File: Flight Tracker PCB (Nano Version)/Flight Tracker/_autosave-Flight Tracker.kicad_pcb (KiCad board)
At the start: 2 copper layers, 101.1 x 78.8 mm, 53 parts, among them J1 Conn_01x02, J2 Conn_01x02, J3 Screw_Terminal_01x02, J4 Conn_01x02, J5 Conn_01x03, J6 Conn_02x03_Odd_Even, Q1 BSS138, Q2 BSS138, Q3 BSS138, Q4 BSS138, Q5 BSS138, Q6 BSS138, Q7 FQP47P06, Q8 BSS138, Q9 BSS138, U1 ML8511, U2 BH1750, U3 SMA_5pin, U4 NTX2_With_Model, U5 BMP280, U6 MPU_9250, U7 UBlox_MAX8

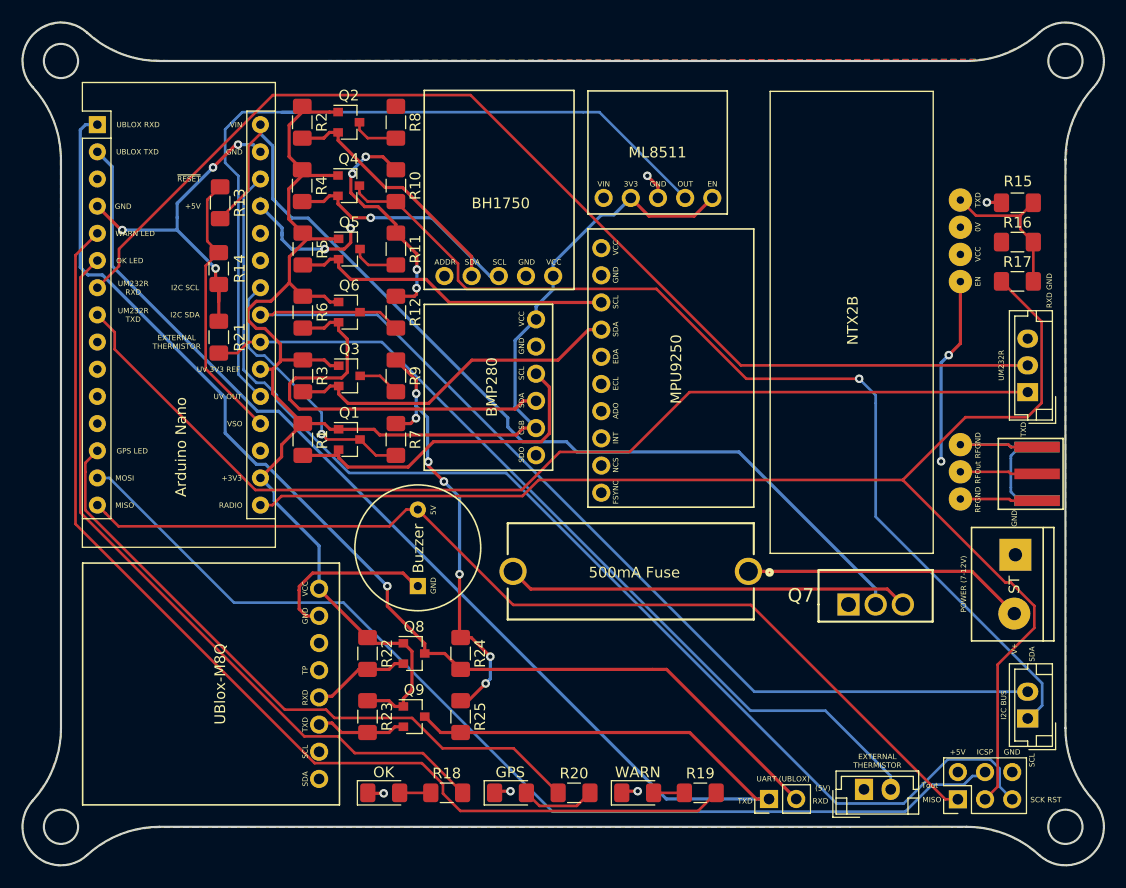
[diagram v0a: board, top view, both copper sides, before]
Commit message: made bmp280 cad model and linked it to pcb, also created sockets for arduino nano
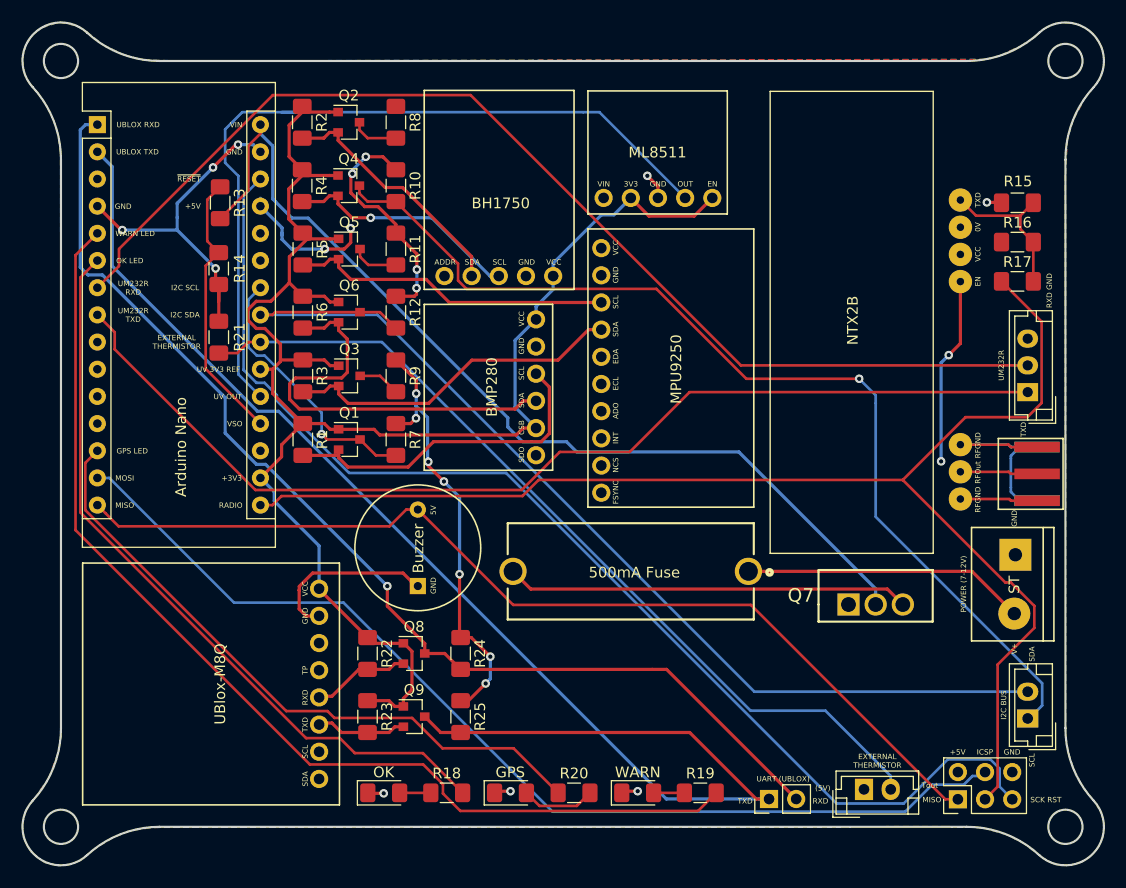
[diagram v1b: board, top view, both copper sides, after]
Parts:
- A1: footprint NTX2:Arduino_Nano_With_Model -> NTX2:Arduino_Nano_With_Model_Sockets

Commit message: Modified a BH1750 CAD model and linked it with footprint
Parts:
- U2: value BH1750 -> BH1750_With_Model; footprint NTX2:BH1750 -> NTX2:BH1750_With_Model
- U5: value BMP280 -> BMP280_With_Model; footprint NTX2:BMP280 -> NTX2:BMP280_With_Model
- U6: value MPU_9250 -> MPU_9250_With_Model; footprint NTX2:MPU_9250 -> NTX2:MPU_9250_With_Model
